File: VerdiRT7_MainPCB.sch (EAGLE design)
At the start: 183 parts, among them J1 RECEPT_SMD_5-2, J2 RECEPT_SMD_5-2, J4 MOLEX_105027, J5 BM06B-SRSS-TB, J8 BM02B-SRSS-TB, J9 BM02B-ZESS-TBT, Q1 AON7934, Q14 AON7934, Q15 AON7934, Q2 AON7934, Q3 AON7934, Q4 AON7934, Q7 SI7615ADN, SW1 AYZ0102AGRLC, SW3 SKRH, SW4 TACT_SWITCHO, U10 RT9625A, U13 MCP1416, U14 MCP1416, U15 MCP1416, U16 MCP6001, U17 MCP6001, U18 RT9625A, U2 MPU-6500, U3 7408_3, U4 RT9625A, U5 MCP6001, U6 MCP1416, U7 7408_3, U8 7408_3, U9 MCP6001, X1 NX3225

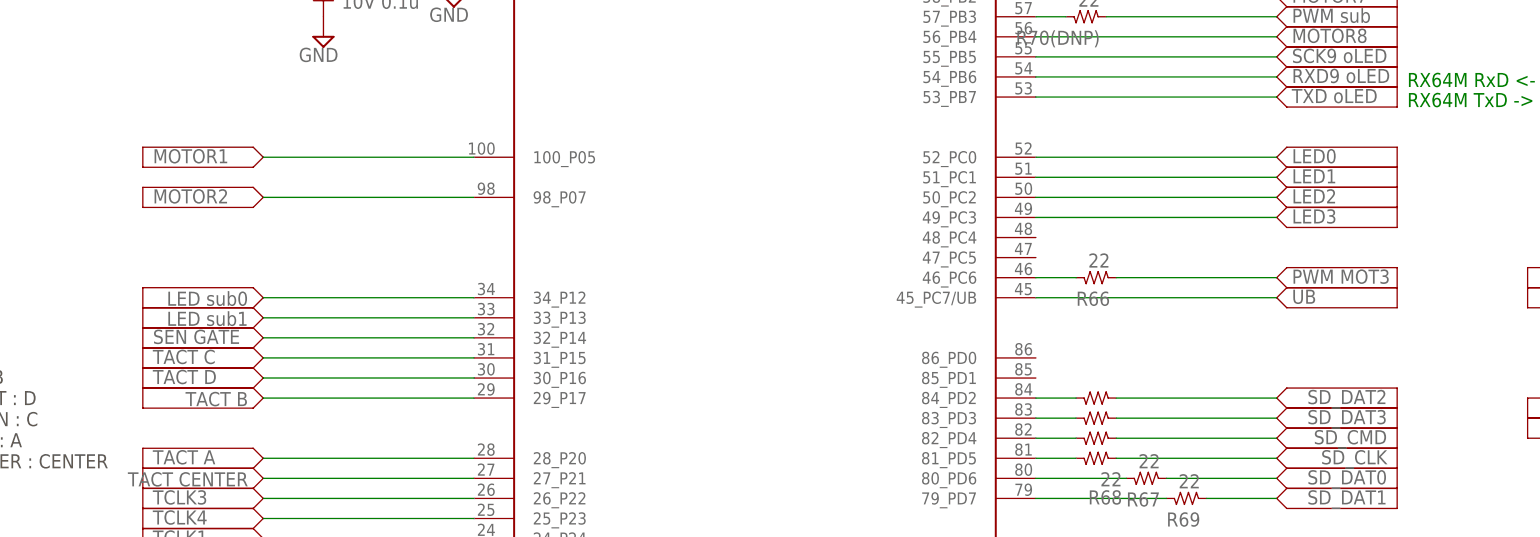
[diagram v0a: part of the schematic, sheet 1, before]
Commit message: updated: AD0 モジュール使用によるピンアサイン変更          P05, P07 を使用しない
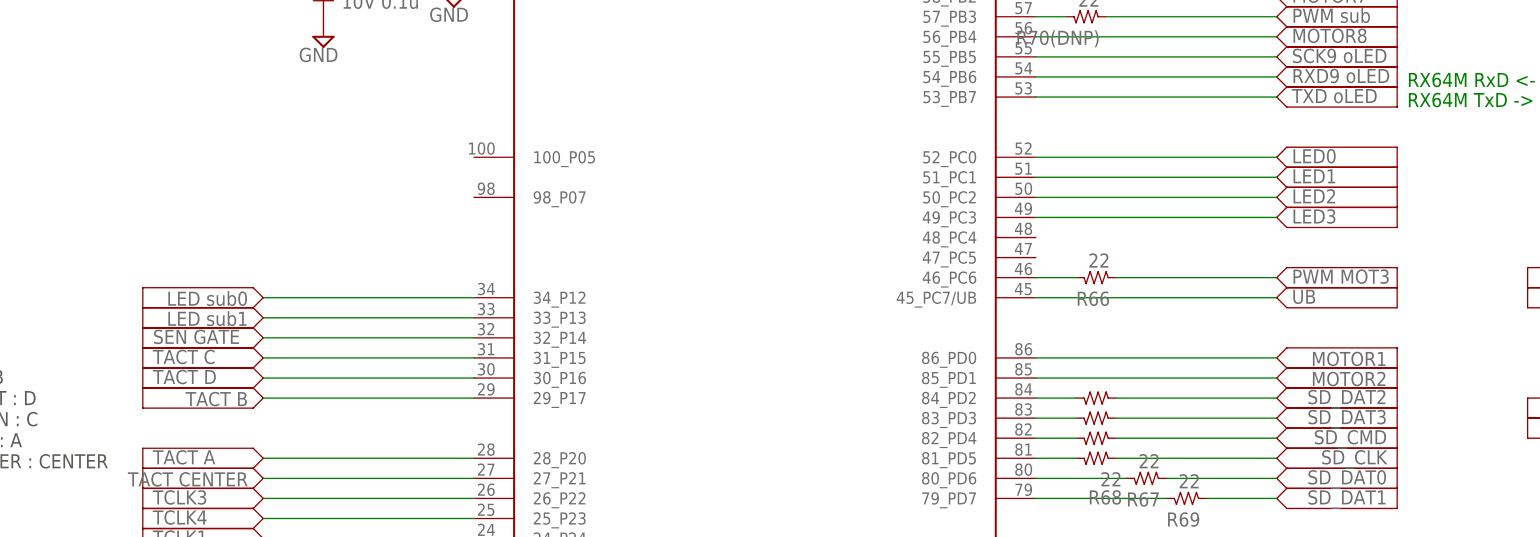
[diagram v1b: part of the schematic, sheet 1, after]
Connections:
- net MOTOR1: now also U1.86_PD0; no longer U1.100_P05
- net MOTOR2: now also U1.85_PD1; no longer U1.98_P07
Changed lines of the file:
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@@
 <setting verticaltext="up"/>
 </settings>
-<grid distance="0.1" unitdist="inch" unit="inch" style="lines" multiple="1" display="no" altdistance="0.01" altunitdist="inch" altunit="inch"/>
+<grid distance="0.05" unitdist="inch" unit="inch" style="lines" multiple="1" display="yes" altdistance="0.01" altunitdist="inch" altunit="inch"/>
 <layers>
 <layer number="1" name="Top" color="4" fill="1" visible="no" active="no"/>
@@
 <instance part="SUPPLY76" gate="G$1" x="148.59" y="74.93"/>
 <instance part="SUPPLY77" gate="G$1" x="148.59" y="72.39"/>
-<instance part="SUPPLY78" gate="G$1" x="148.59" y="118.11"/>
+<instance part="SUPPLY78" gate="G$1" x="307.34" y="92.71" rot="R180"/>
 <instance part="SUPPLY79" gate="G$1" x="307.34" y="64.77" rot="R180"/>
 <instance part="SUPPLY81" gate="G$1" x="307.34" y="67.31" rot="R180"/>
@@
 <instance part="SUPPLY199" gate="G$1" x="307.34" y="166.37"/>
 <instance part="SUPPLY200" gate="G$1" x="307.34" y="168.91"/>
-<instance part="SUPPLY201" gate="G$1" x="148.59" y="113.03"/>
+<instance part="SUPPLY201" gate="G$1" x="307.34" y="90.17" rot="R180"/>
 <instance part="SUPPLY202" gate="G$1" x="307.34" y="59.69" rot="R180"/>
 <instance part="SUPPLY203" gate="G$1" x="307.34" y="138.43"/>
@@
 <net name="MOTOR1" class="0">
 <segment>
-<wire x1="190.5" y1="118.11" x2="163.83" y2="118.11" width="0.1524" layer="91"/>
+<wire x1="261.62" y1="92.71" x2="292.1" y2="92.71" width="0.1524" layer="91"/>
 <pinref part="SUPPLY78" gate="G$1" pin="P$1"/>
-<pinref part="U1" gate="G$1" pin="100_P05"/>
+<pinref part="U1" gate="G$1" pin="86_PD0"/>
 </segment>
 </net>
@@
 <net name="MOTOR2" class="0">
 <segment>
-<wire x1="163.83" y1="113.03" x2="190.5" y2="113.03" width="0.1524" layer="91"/>
+<wire x1="292.1" y1="90.17" x2="261.62" y2="90.17" width="0.1524" layer="91"/>
 <pinref part="SUPPLY201" gate="G$1" pin="P$1"/>
-<pinref part="U1" gate="G$1" pin="98_P07"/>
-</segment>
-</net>
+<pinref part="U1" gate="G$1" pin="85_PD1"/>
+</segment>
+</net>

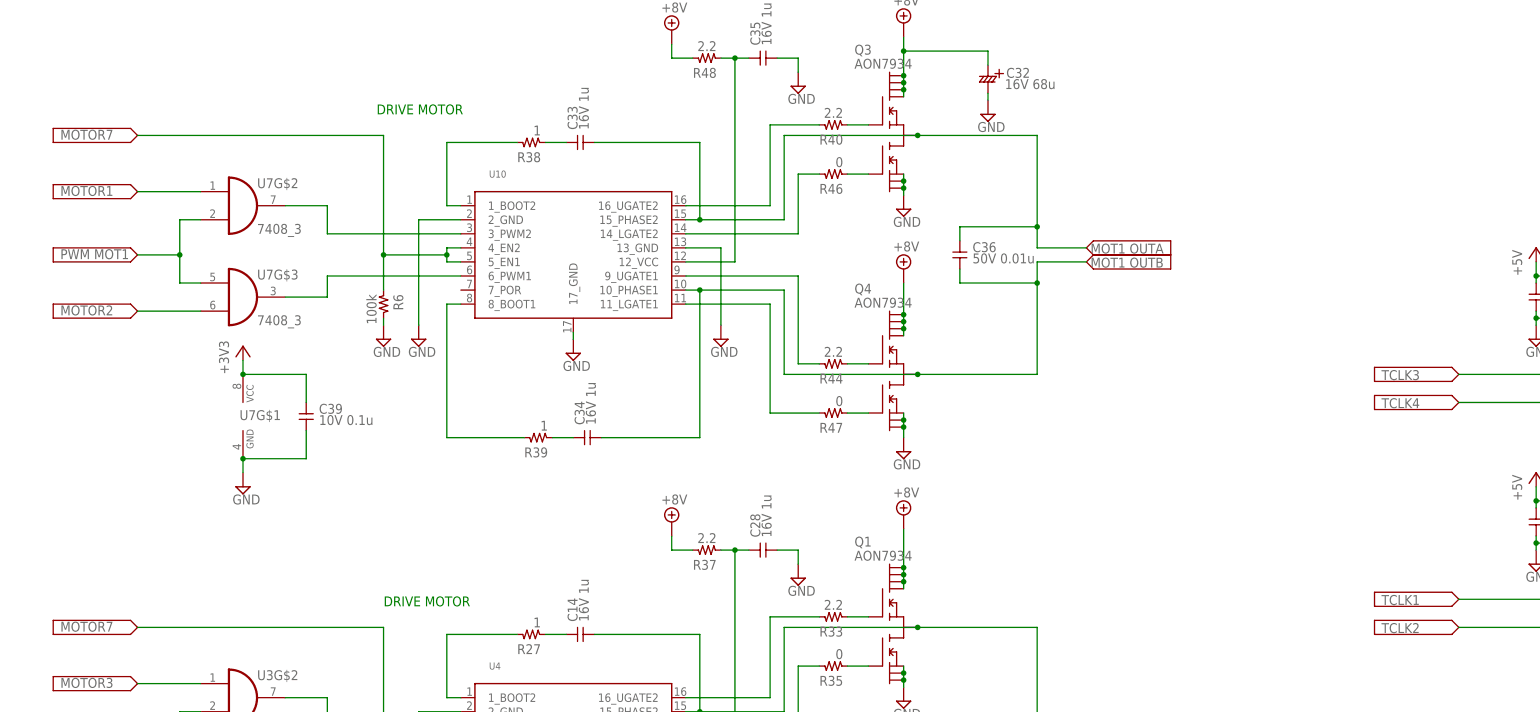
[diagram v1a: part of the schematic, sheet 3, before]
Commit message: updated: schematic にコメント挿入
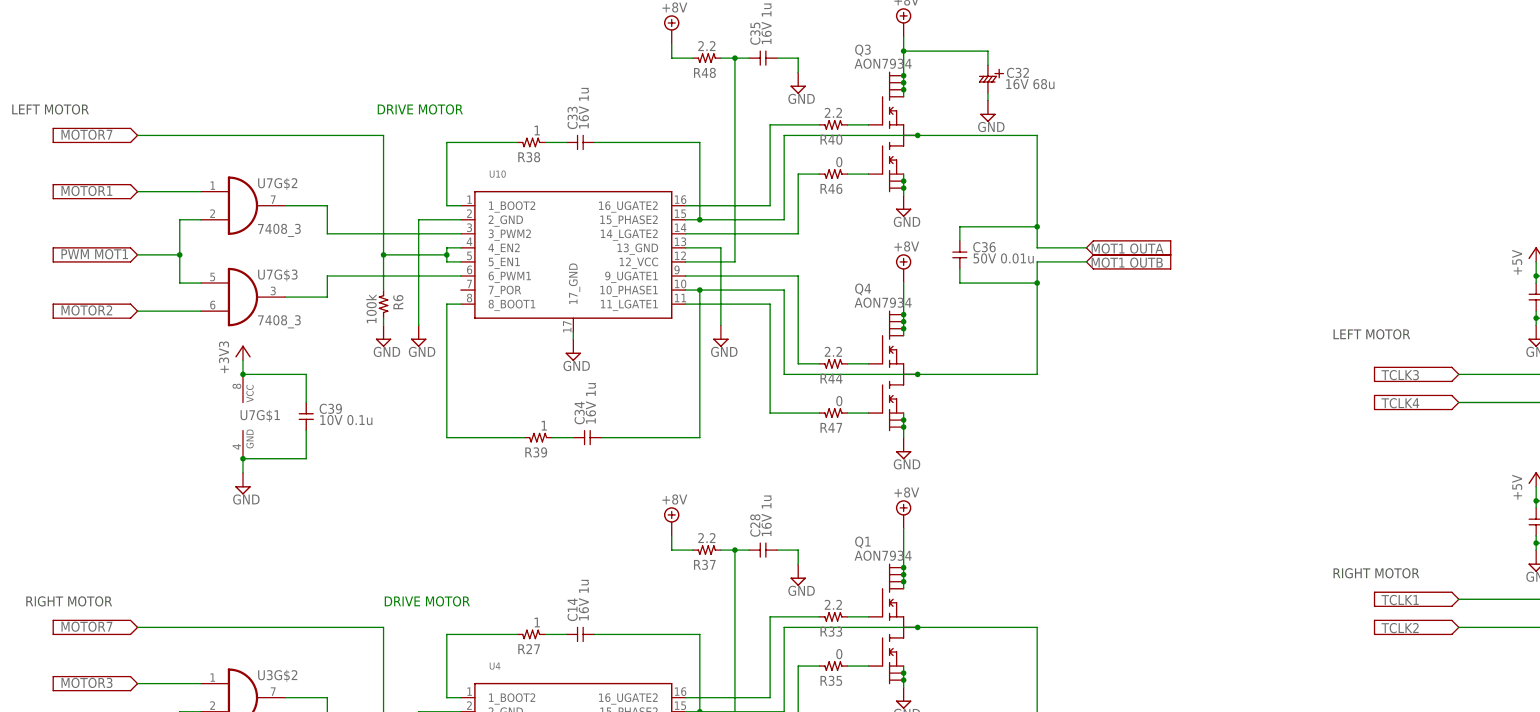
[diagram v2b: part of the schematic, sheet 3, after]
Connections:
- net N$86 renamed PWM_MOT1_MPU
- net N$87 renamed PWM_MOT2_MPU
- net N$88 renamed PWM_MOT3_MPU
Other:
- note added: "LEFT MOTOR"
- note added: "Left Marker"
- note added: "RIGHT MOTOR"
- note added: "Right Marker"
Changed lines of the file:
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@@
 <setting verticaltext="up"/>
 </settings>
-<grid distance="0.05" unitdist="inch" unit="inch" style="lines" multiple="1" display="yes" altdistance="0.01" altunitdist="inch" altunit="inch"/>
+<grid distance="0.05" unitdist="inch" unit="inch" style="lines" multiple="1" display="no" altdistance="0.01" altunitdist="inch" altunit="inch"/>
 <layers>
 <layer number="1" name="Top" color="4" fill="1" visible="no" active="no"/>
@@
 LEFT : A
 CENTER : CENTER</text>
+<text x="129.54" y="72.39" size="1.778" layer="97">LEFT MOTOR</text>
+<text x="129.54" y="67.31" size="1.778" layer="97">RIGHT MOTOR</text>
 </plain>
 <instances>
@@
 </segment>
 </net>
-<net name="N$86" class="0">
+<net name="PWM_MOT1_MPU" class="0">
 <segment>
 <wire x1="264.16" y1="64.77" x2="261.62" y2="64.77" width="0.1524" layer="91"/>
@@
 </segment>
 </net>
-<net name="N$87" class="0">
+<net name="PWM_MOT2_MPU" class="0">
 <segment>
 <wire x1="270.51" y1="62.23" x2="261.62" y2="62.23" width="0.1524" layer="91"/>
@@
 </segment>
 </net>
-<net name="N$88" class="0">
+<net name="PWM_MOT3_MPU" class="0">
 <segment>
 <wire x1="261.62" y1="102.87" x2="266.7" y2="102.87" width="0.1524" layer="91"/>
@@
 <text x="335.28" y="149.86" size="1.778" layer="97">9: MOT OUT A</text>
 <text x="335.28" y="147.32" size="1.778" layer="97">10: MOT OUT B</text>
+<text x="236.22" y="165.1" size="1.778" layer="97">RIGHT MOTOR</text>
+<text x="236.22" y="208.28" size="1.778" layer="97">LEFT MOTOR</text>
+<text x="-2.54" y="248.92" size="1.778" layer="97">LEFT MOTOR</text>
+<text x="0" y="160.02" size="1.778" layer="97">RIGHT MOTOR</text>
 </plain>
 <instances>
@@
 <text x="100.33" y="39.37" size="1.778" layer="91">5.GND</text>
 <text x="100.33" y="36.83" size="1.778" layer="91">6.Sensor AD</text>
+<text x="124.46" y="137.16" size="1.778" layer="97">Left Marker</text>
+<text x="124.46" y="50.8" size="1.778" layer="97">Right Marker</text>
 </plain>
 <instances>

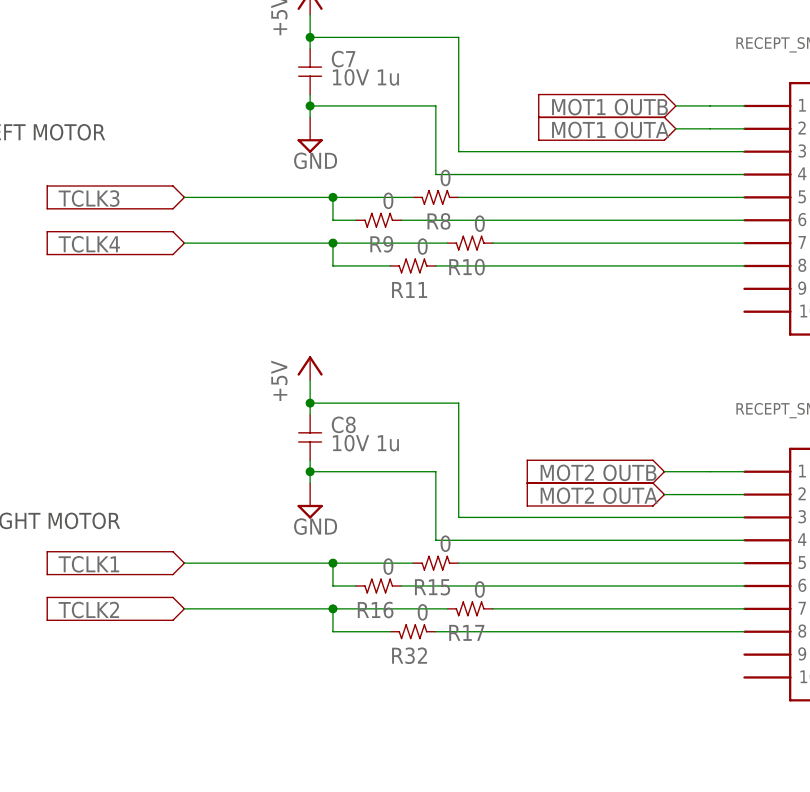
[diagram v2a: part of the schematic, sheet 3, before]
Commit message: updated: Bluetooth モジュールの電源を+5V -> +3.3V に変更
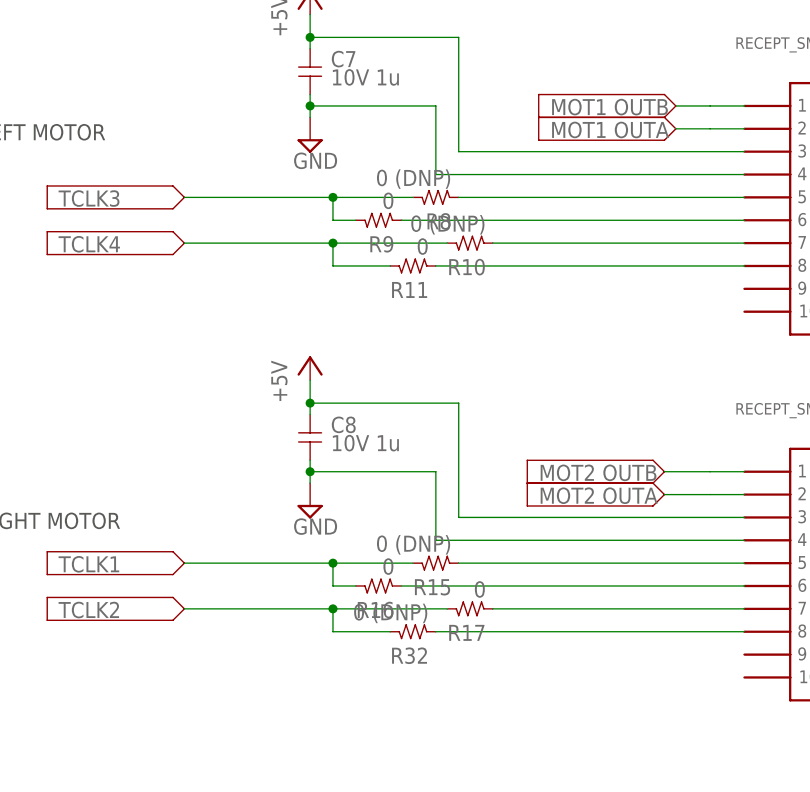
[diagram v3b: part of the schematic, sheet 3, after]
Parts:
- R10, R15, R32, R8: value 0 -> 0 (DNP)
- R21, R22: value 20k -> 20k (DNP)
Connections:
- net +3V3: now also C53.P$1, CH1.1, R75(DNP).P$2, R76(DNP).P$2
- net +5V: no longer C53.P$1, CH1.1, R75(DNP).P$2, R76(DNP).P$2
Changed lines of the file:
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@@
 <part name="SUPPLY98" library="supply2" deviceset="GND" device=""/>
 <part name="C27" library="capacitor" deviceset="1005" device="" value="10V 0.1u"/>
-<part name="R21" library="resistor" deviceset="R" device="1005" value="20k"/>
-<part name="R22" library="resistor" deviceset="R" device="1005" value="20k"/>
+<part name="R21" library="resistor" deviceset="R" device="1005" value="20k (DNP)"/>
+<part name="R22" library="resistor" deviceset="R" device="1005" value="20k (DNP)"/>
 <part name="SUPPLY151" library="supply2" deviceset="V&lt;--" device="" value="MD/FINE"/>
 <part name="SUPPLY152" library="supply2" deviceset="V&lt;--" device="" value="RESET"/>
@@
 <part name="R75(DNP)" library="resistor" deviceset="R" device="1005" value="20k"/>
 <part name="R76(DNP)" library="resistor" deviceset="R" device="1005" value="20k"/>
-<part name="P+3" library="supply1" deviceset="+5V" device=""/>
 <part name="C53" library="capacitor" deviceset="1005" device="" value="10V 0.1u"/>
 <part name="C54" library="capacitor" deviceset="1005" device="" value="10V 0.1u"/>
@@
 <part name="C8" library="capacitor" deviceset="1005" device="" value="10V 1u"/>
 <part name="SUPPLY111" library="supply2" deviceset="GND" device=""/>
-<part name="R15" library="resistor" deviceset="R" device="1005" value="0"/>
+<part name="R15" library="resistor" deviceset="R" device="1005" value="0 (DNP)"/>
 <part name="R16" library="resistor" deviceset="R" device="1005" value="0"/>
 <part name="R17" library="resistor" deviceset="R" device="1005" value="0"/>
-<part name="R32" library="resistor" deviceset="R" device="1005" value="0"/>
+<part name="R32" library="resistor" deviceset="R" device="1005" value="0 (DNP)"/>
 <part name="SUPPLY112" library="supply2" deviceset="V--&gt;" device="" value="TCLK3"/>
 <part name="SUPPLY113" library="supply2" deviceset="V--&gt;" device="" value="TCLK4"/>
@@
 <part name="C7" library="capacitor" deviceset="1005" device="" value="10V 1u"/>
 <part name="SUPPLY115" library="supply2" deviceset="GND" device=""/>
-<part name="R8" library="resistor" deviceset="R" device="1005" value="0"/>
+<part name="R8" library="resistor" deviceset="R" device="1005" value="0 (DNP)"/>
 <part name="R9" library="resistor" deviceset="R" device="1005" value="0"/>
-<part name="R10" library="resistor" deviceset="R" device="1005" value="0"/>
+<part name="R10" library="resistor" deviceset="R" device="1005" value="0 (DNP)"/>
 <part name="R11" library="resistor" deviceset="R" device="1005" value="0"/>
 <part name="SUPPLY118" library="supply2" deviceset="V--&gt;" device="" value="MOTOR7"/>
@@
 <part name="SUPPLY227" library="supply2" deviceset="V--&gt;" device="" value="G_INT"/>
 <part name="R63" library="resistor" deviceset="R" device="1005" value="22"/>
+<part name="+3V3_LED16" library="supply1" deviceset="+3V3" device=""/>
 </parts>
 <sheets>
@@
 <instance part="R75(DNP)" gate="G$1" x="453.39" y="132.08" rot="R90"/>
 <instance part="R76(DNP)" gate="G$1" x="445.77" y="132.08" rot="R90"/>
-<instance part="P+3" gate="1" x="459.74" y="151.13"/>
 <instance part="C53" gate="G$1" x="464.82" y="143.51"/>
 <instance part="C54" gate="G$1" x="466.09" y="190.5"/>
@@
 <instance part="J4" gate="G$1" x="430.53" y="81.28"/>
 <instance part="SUPPLY252" gate="GND" x="369.57" y="107.95"/>
+<instance part="+3V3_LED16" gate="G$1" x="459.74" y="151.13"/>
 </instances>
 <busses>
@@
 <pinref part="R41" gate="G$1" pin="R4-B"/>
 <pinref part="R41" gate="G$1" pin="R3-B"/>
-</segment>
-<segment>
-<wire x1="459.74" y1="148.59" x2="459.74" y2="146.05" width="0.1524" layer="91"/>
-<wire x1="459.74" y1="146.05" x2="459.74" y2="137.16" width="0.1524" layer="91"/>
-<wire x1="459.74" y1="137.16" x2="459.74" y2="133.35" width="0.1524" layer="91"/>
-<wire x1="453.39" y1="134.62" x2="453.39" y2="137.16" width="0.1524" layer="91"/>
-<wire x1="453.39" y1="137.16" x2="459.74" y2="137.16" width="0.1524" layer="91"/>
-<wire x1="445.77" y1="134.62" x2="445.77" y2="137.16" width="0.1524" layer="91"/>
-<wire x1="445.77" y1="137.16" x2="453.39" y2="137.16" width="0.1524" layer="91"/>
-<wire x1="459.74" y1="133.35" x2="466.09" y2="133.35" width="0.1524" layer="91"/>
-<wire x1="464.82" y1="146.05" x2="459.74" y2="146.05" width="0.1524" layer="91"/>
-<junction x="459.74" y="137.16"/>
-<junction x="453.39" y="137.16"/>
-<junction x="459.74" y="146.05"/>
-<pinref part="R75(DNP)" gate="G$1" pin="P$2"/>
-<pinref part="R76(DNP)" gate="G$1" pin="P$2"/>
-<pinref part="P+3" gate="1" pin="+5V"/>
-<pinref part="CH1" gate="G$1" pin="1"/>
-<pinref part="C53" gate="G$1" pin="P$1"/>
 </segment>
 </net>
@@
 <pinref part="+3V3_LED22" gate="G$1" pin="+3V3"/>
 </segment>
-</net>
+<segment>
+<wire x1="459.74" y1="148.59" x2="459.74" y2="146.05" width="0.1524" layer="91"/>
+<wire x1="459.74" y1="146.05" x2="459.74" y2="137.16" width="0.1524" layer="91"/>
+<wire x1="459.74" y1="137.16" x2="459.74" y2="133.35" width="0.1524" layer="91"/>
+<wire x1="453.39" y1="134.62" x2="453.39" y2="137.16" width="0.1524" layer="91"/>
+<wire x1="453.39" y1="137.16" x2="459.74" y2="137.16" width="0.1524" layer="91"/>
+<wire x1="445.77" y1="134.62" x2="445.77" y2="137.16" width="0.1524" layer="91"/>
+<wire x1="445.77" y1="137.16" x2="453.39" y2="137.16" width="0.1524" layer="91"/>
+<wire x1="459.74" y1="133.35" x2="466.09" y2="133.35" width="0.1524" layer="91"/>
+<wire x1="464.82" y1="146.05" x2="459.74" y2="146.05" width="0.1524" layer="91"/>
+<junction x="459.74" y="137.16"/>
+<junction x="453.39" y="137.16"/>
+<junction x="459.74" y="146.05"/>
+<pinref part="R75(DNP)" gate="G$1" pin="P$2"/>
+<pinref part="R76(DNP)" gate="G$1" pin="P$2"/>
+<pinref part="CH1" gate="G$1" pin="1"/>
+<pinref part="C53" gate="G$1" pin="P$1"/>
+<pinref part="+3V3_LED16" gate="G$1" pin="+3V3"/>
+</segment>
+</net>
